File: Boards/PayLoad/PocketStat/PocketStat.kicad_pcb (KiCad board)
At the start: 4 copper layers, 40 x 40 mm, 75 parts, among them IC1 HDC3022QDEJRQ1, J1 BM03B-SRSS-TBLFSN, J10 Conn_01x01_Socket, J11 Conn_01x01_Socket, J12 Conn_01x01_Socket, J13 Conn_01x01_Socket, J14 Conn_01x01_Socket, J15 Conn_01x01_Socket, J16 Conn_01x01_Socket, J17 Conn_01x01_Socket, J18 Conn_01x01_Socket, J19 Conn_01x01_Socket, J2 Conn_01x01_Socket, J3 DX07S016JA1R1500, J4 MEM2061-01-188-00-A_REVA, J5 Conn_01x01_Socket, J6 Conn_01x01_Socket, J7 Conn_01x01_Socket, J8 Conn_01x01_Socket, J9 Conn_01x01_Socket, SW1 D2F-01-D, U4 LPS22DFTR, U5 W25Q128JVSIQ TR, U6 BMP581, U7 ESD7L5.0DT5G, U8 ST1L05APU33R

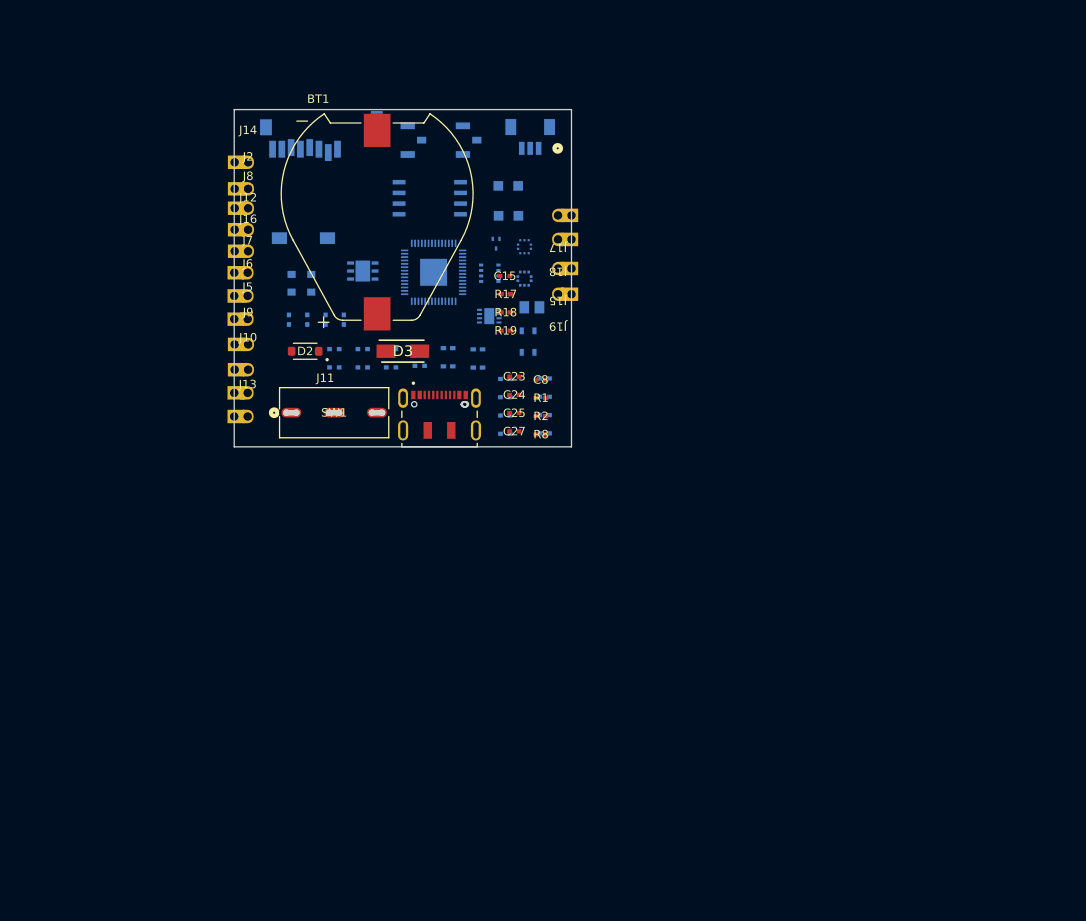
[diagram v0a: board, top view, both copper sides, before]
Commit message: Recomecei o PCB da Pocket Stat
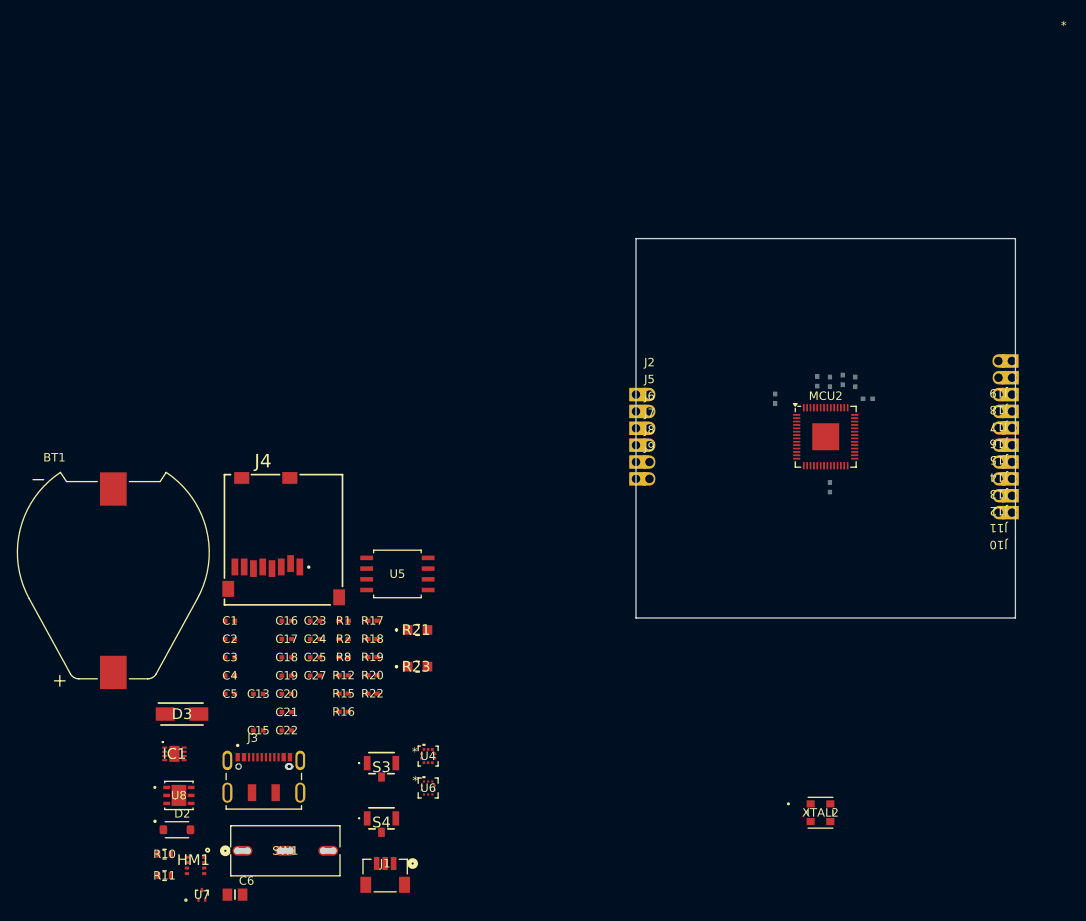
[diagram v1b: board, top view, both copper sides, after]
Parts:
- C1, C13, C16, C17, C18, C19, C2, C20, C21, C22, C3, C4, C5, C6, HM1, IC1, J1, J4, MCU2, R10, R11, R12, R15, R16, R20, R21, R22, R23, S3, S4, U4, U5, U6, U7, U8, XTAL2: moved to F.Cu
- C8: moved to B.Cu
- moved J14 95.1 mm to (169.0, 72.0), turned to 180 degrees
- moved J12 93.8 mm to (169.0, 76.0), turned to 180 degrees
- moved J16 91.0 mm to (169.0, 68.0), turned to 180 degrees
- moved J10 90.6 mm to (169.0, 80.0), turned to 180 degrees
- moved J11 89.9 mm to (169.0, 78.0), turned to 180 degrees
- moved J1 89.3 mm to (96.2, 123.0)
- moved J13 89.2 mm to (169.0, 74.0), turned to 180 degrees
- moved XTAL2 87.9 mm to (147.9, 115.6)
- moved U7 84.7 mm to (74.5, 125.3)
- moved S4 81.0 mm to (95.8, 116.3), turned to 0 degrees
- moved C6 78.0 mm to (78.4, 125.3)
- moved R11 77.7 mm to (70.1, 123.1)
- moved HM1 76.7 mm to (72.7, 120.9)
- moved S3 74.0 mm to (95.8, 109.7), turned to 0 degrees
- moved R10 73.5 mm to (70.1, 120.5)
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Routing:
- added copper zone on In2.Cu, net GND
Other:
- board size 40 x 40 mm -> 45 x 45 mm
